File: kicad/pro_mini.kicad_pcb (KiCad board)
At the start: 2 copper layers, 17.8 x 33 mm, 15 parts, among them IC1 ATMEGA328P-A, P1 FTDI, P2 DIGITAL, P3 CONN_01X12, U1 MCP1700T-3302E

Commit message: Back silkscreen
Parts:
- added REF**: TheApiLogo, theapi_graphics:TheApiLogo, B.Cu at (110.9, 107.3)
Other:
- board text added: "3V3 8MHz internal oscillator"
- board text added: "https://github.com/theapi/pro_mini"
- board text added: "v1.0"
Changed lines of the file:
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@@
 (kicad_pcb (version 4) (host pcbnew 4.0.1-stable)
   (general
-    (links 0)
+    (links 54)
     (no_connects 0)
-    (area 99.799724 94.0002 123.323134 136.9898)
+    (area 101.524999 98.984999 119.455001 132.155001)
     (thickness 1.6)
-    (drawings 34)
+    (drawings 37)
     (tracks 280)
     (zones 0)
-    (modules 15)
+    (modules 16)
     (nets 32)
   )
   (page A4)
   (layers
-    (0 F.Cu signal)
-    (31 B.Cu signal)
+    (0 F.Cu signal hide)
+    (31 B.Cu signal hide)
     (32 B.Adhes user)
     (33 F.Adhes user)
@@
     (pad_to_mask_clearance 0.2)
     (aux_axis_origin 0 0)
-    (visible_elements 7FFFFFFF)
+    (visible_elements 7FFFFDFF)
     (pcbplotparams
       (layerselection 0x010f0_80000001)
@@
     (fp_circle (center 0.12 2.2) (end 0.15 2.21) (layer F.Mask) (width 0.15))
   )
+  (module theapi_graphics:TheApiLogo (layer B.Cu)
+    (at 110.871 107.315 180)
+    (fp_text reference REF** (at -1.45 -16.875 180) (layer B.SilkS) hide
+      (effects (font (size 1 1) (thickness 0.15)) (justify mirror))
+    )
+    (fp_text value TheApiLogo (at 0 0.5 180) (layer B.Fab)
+      (effects (font (size 1 1) (thickness 0.15)) (justify mirror))
+    )
+    (fp_line (start 2.575 -21.95) (end 3.3 -20.725) (layer B.SilkS) (width 0.15))
+    (fp_line (start 3.3 -20.725) (end 3.55 -19.725) (layer B.SilkS) (width 0.15))
+    (fp_line (start 3.55 -19.725) (end 3.925 -21.25) (layer B.SilkS) (width 0.15))
+    (fp_line (start 3.925 -21.25) (end 3.375 -22.325) (layer B.SilkS) (width 0.15))
+    (fp_line (start 3.375 -22.325) (end 2.5 -23.475) (layer B.SilkS) (width 0.15))
+    (fp_line (start 2.5 -23.475) (end 2.85 -23.3) (layer B.SilkS) (width 0.15))
+    (fp_line (start 0.35 -9.95) (end 1.25 -12.275) (layer B.SilkS) (width 0.15))
+    (fp_line (start 1.25 -12.275) (end 2.05 -13.5) (layer B.SilkS) (width 0.15))
+    (fp_line (start 2.05 -13.5) (end 2.575 -15.025) (layer B.SilkS) (width 0.15))
+    (fp_line (start 2.575 -15.025) (end 2.85 -16.725) (layer B.SilkS) (width 0.15))
+    (fp_line (start 2.85 -16.725) (end 2.95 -18.575) (layer B.SilkS) (width 0.15))
+    (fp_line (start 2.95 -18.575) (end 2.675 -20.625) (layer B.SilkS) (width 0.15))
+    (fp_line (start 2.675 -20.625) (end 2.5 -23.025) (layer B.SilkS) (width 0.15))
+    (fp_line (start 2.5 -23.025) (end 2.05 -24.525) (layer B.SilkS) (width 0.15))
+    (fp_line (start 2.05 -24.525) (end 2.05 -24.9) (layer B.SilkS) (width 0.15))
+    (fp_line (start -1.025 -7.525) (end -0.7 -8.05) (layer B.SilkS) (width 0.15))
+    (fp_line (start -0.7 -8.05) (end -0.25 -8.25) (layer B.SilkS) (width 0.15))
+    (fp_line (start -0.25 -8.25) (end 0.325 -8.475) (layer B.SilkS) (width 0.15))
+    (fp_line (start 0.325 -8.475) (end 1.1 -8.6) (layer B.SilkS) (width 0.15))
+    (fp_line (start 1.1 -8.6) (end 1.725 -8.375) (layer B.SilkS) (width 0.15))
+    (fp_line (start 1.725 -8.375) (end 2.15 -7.975) (layer B.SilkS) (width 0.15))
+    (fp_line (start 2.15 -7.975) (end 2.325 -7.3) (layer B.SilkS) (width 0.15))
+    (fp_line (start 2.325 -7.3) (end 2.225 -7.3) (layer B.SilkS) (width 0.15))
+    (fp_line (start 1.55 -5.7) (end 1.05 -5.75) (layer B.SilkS) (width 0.15))
+    (fp_line (start 1.05 -5.75) (end 0.925 -6.075) (layer B.SilkS) (width 0.15))
+    (fp_line (start 0.925 -6.075) (end 0.975 -6.525) (layer B.SilkS) (width 0.15))
+    (fp_line (start 0.975 -6.525) (end 1.6 -6.575) (layer B.SilkS) (width 0.15))
+    (fp_line (start 1.6 -6.575) (end 1.875 -6.3) (layer B.SilkS) (width 0.15))
+    (fp_line (start 1.875 -6.3) (end 1.55 -5.975) (layer B.SilkS) (width 0.15))
+    (fp_line (start -0.7 -5.7) (end -1.025 -5.925) (layer B.SilkS) (width 0.15))
+    (fp_line (start -1.025 -5.925) (end -1.025 -6.575) (layer B.SilkS) (width 0.15))
+    (fp_line (start -1.025 -6.575) (end -0.475 -6.575) (layer B.SilkS) (width 0.15))
+    (fp_line (start -0.475 -6.575) (end -0.075 -6.425) (layer B.SilkS) (width 0.15))
+    (fp_line (start -0.075 -6.425) (end -0.125 -6.025) (layer B.SilkS) (width 0.15))
+    (fp_line (start -0.125 -6.025) (end -0.4 -5.975) (layer B.SilkS) (width 0.15))
+    (fp_line (start -0.4 -5.975) (end -0.7 -5.8) (layer B.SilkS) (width 0.15))
+    (fp_line (start -0.7 -5.8) (end -0.4 -5.8) (layer B.SilkS) (width 0.15))
+    (fp_line (start 4.05 -9.5) (end 3.625 -9) (layer B.SilkS) (width 0.15))
+    (fp_line (start 3.625 -9) (end 2.725 -8.6) (layer B.SilkS) (width 0.15))
+    (fp_line (start 2.725 -8.6) (end 3.825 -8.6) (layer B.SilkS) (width 0.15))
+    (fp_line (start 3.825 -8.6) (end 5.3 -8.15) (layer B.SilkS) (width 0.15))
+    (fp_line (start 5.3 -8.15) (end 6.175 -7.6) (layer B.SilkS) (width 0.15))
+    (fp_line (start 6.175 -7.6) (end 6.475 -6.8) (layer B.SilkS) (width 0.15))
+    (fp_line (start 6.475 -6.8) (end 6.4 -6.15) (layer B.SilkS) (width 0.15))
+    (fp_line (start 6.4 -6.15) (end 6.125 -5.7) (layer B.SilkS) (width 0.15))
+    (fp_line (start 6.125 -5.7) (end 5.45 -5.25) (layer B.SilkS) (width 0.15))
+    (fp_line (start 5.45 -5.25) (end 4.775 -5.2) (layer B.SilkS) (width 0.15))
+    (fp_line (start 4.775 -5.2) (end 3.9 -5.125) (layer B.SilkS) (width 0.15))
+    (fp_line (start 3.9 -5.125) (end 3.225 -5.125) (layer B.SilkS) (width 0.15))
+    (fp_line (start 3.225 -5.125) (end 2.825 -5.125) (layer B.SilkS) (width 0.15))
+    (fp_line (start 2.825 -5.125) (end 2.825 -5.075) (layer B.SilkS) (width 0.15))
+    (fp_line (start -2.15 -5.575) (end -3.15 -5.75) (layer B.SilkS) (width 0.15))
+    (fp_line (start -3.15 -5.75) (end -3.875 -5.925) (layer B.SilkS) (width 0.15))
+    (fp_line (start -3.875 -5.925) (end -4.65 -6.35) (layer B.SilkS) (width 0.15))
+    (fp_line (start -4.65 -6.35) (end -5.325 -6.925) (layer B.SilkS) (width 0.15))
+    (fp_line (start -5.325 -6.925) (end -5.45 -8.1) (layer B.SilkS) (width 0.15))
+    (fp_line (start -5.45 -8.1) (end -5 -9) (layer B.SilkS) (width 0.15))
+    (fp_line (start -5 -9) (end -4.15 -9.375) (layer B.SilkS) (width 0.15))
+    (fp_line (start -4.15 -9.375) (end -3.1 -9.275) (layer B.SilkS) (width 0.15))
+    (fp_line (start -3.1 -9.275) (end -2.475 -8.875) (layer B.SilkS) (width 0.15))
+    (fp_line (start -2.475 -8.875) (end -2.025 -8.6) (layer B.SilkS) (width 0.15))
+    (fp_line (start -2.025 -8.6) (end -2.525 -9.325) (layer B.SilkS) (width 0.15))
+    (fp_line (start -2.525 -9.325) (end -2.925 -10.55) (layer B.SilkS) (width 0.15))
+    (fp_line (start -2.925 -10.55) (end -2.7 -11.45) (layer B.SilkS) (width 0.15))
+    (fp_line (start -2.7 -11.45) (end -2.2 -12.225) (layer B.SilkS) (width 0.15))
+    (fp_line (start -2.2 -12.225) (end -1.35 -12.35) (layer B.SilkS) (width 0.15))
+    (fp_line (start -1.35 -12.35) (end -0.175 -12.125) (layer B.SilkS) (width 0.15))
+    (fp_line (start -0.175 -12.125) (end 0.25 -11.5) (layer B.SilkS) (width 0.15))
+    (fp_line (start 0.25 -11.5) (end 0.425 -10.775) (layer B.SilkS) (width 0.15))
+    (fp_line (start 0.425 -10.775) (end 0.375 -9.95) (layer B.SilkS) (width 0.15))
+    (fp_line (start 0.375 -9.95) (end 0.825 -10.675) (layer B.SilkS) (width 0.15))
+    (fp_line (start 0.825 -10.675) (end 1.275 -11.225) (layer B.SilkS) (width 0.15))
+    (fp_line (start 1.275 -11.225) (end 2.375 -11.85) (layer B.SilkS) (width 0.15))
+    (fp_line (start 2.375 -11.85) (end 3.5 -11.775) (layer B.SilkS) (width 0.15))
+    (fp_line (start 3.5 -11.775) (end 4.4 -11) (layer B.SilkS) (width 0.15))
+    (fp_line (start 4.4 -11) (end 4.45 -10.15) (layer B.SilkS) (width 0.15))
+    (fp_line (start 4.45 -10.15) (end 4 -9.425) (layer B.SilkS) (width 0.15))
+    (fp_line (start 0.425 -3.95) (end -0.025 -3.175) (layer B.SilkS) (width 0.15))
+    (fp_line (start -0.025 -3.175) (end -0.7 -2.625) (layer B.SilkS) (width 0.15))
+    (fp_line (start -0.7 -2.625) (end -1.475 -2.125) (layer B.SilkS) (width 0.15))
+    (fp_line (start -1.475 -2.125) (end -2.875 -2) (layer B.SilkS) (width 0.15))
+    (fp_line (start -2.875 -2) (end -3.775 -2.45) (layer B.SilkS) (width 0.15))
+    (fp_line (start -3.775 -2.45) (end -4.325 -3.3) (layer B.SilkS) (width 0.15))
+    (fp_line (start -4.325 -3.3) (end -4.275 -4.3) (layer B.SilkS) (width 0.15))
+    (fp_line (start -4.275 -4.3) (end -3.65 -5.125) (layer B.SilkS) (width 0.15))
+    (fp_line (start -3.65 -5.125) (end -2.875 -5.3) (layer B.SilkS) (width 0.15))
+    (fp_line (start -2.875 -5.3) (end -2.025 -5.475) (layer B.SilkS) (width 0.15))
+    (fp_line (start -2.025 -5.475) (end -2.075 -5.7) (layer B.SilkS) (width 0.15))
+    (fp_line (start 0.475 -3.95) (end 0.65 -2.9) (layer B.SilkS) (width 0.15))
+    (fp_line (start 0.65 -2.9) (end 1.15 -2) (layer B.SilkS) (width 0.15))
+    (fp_line (start 1.15 -2) (end 2.375 -1.325) (layer B.SilkS) (width 0.15))
+    (fp_line (start 2.375 -1.325) (end 3.775 -1.45) (layer B.SilkS) (width 0.15))
+    (fp_line (start 3.775 -1.45) (end 4.625 -2.225) (layer B.SilkS) (width 0.15))
+    (fp_line (start 4.625 -2.225) (end 4.85 -3.35) (layer B.SilkS) (width 0.15))
+    (fp_line (start 4.85 -3.35) (end 4.225 -4.3) (layer B.SilkS) (width 0.15))
+    (fp_line (start 4.225 -4.3) (end 3.4 -4.9) (layer B.SilkS) (width 0.15))
+    (fp_line (start 3.4 -4.9) (end 2.775 -5.125) (layer B.SilkS) (width 0.15))
+    (fp_circle (center 0.4 -6.87) (end 2.94 -5.6) (layer B.SilkS) (width 0.15))
+  )
+  (gr_text v1.0 (at 110.744 130.937 360) (layer B.SilkS)
+    (effects (font (size 1.016 1.016) (thickness 0.2032)) (justify mirror))
+  )
+  (gr_text "3V3 8MHz\ninternal\noscillator" (at 110.49 104.775) (layer B.SilkS)
+    (effects (font (size 1.016 1.016) (thickness 0.2032)) (justify mirror))
+  )
+  (gr_text https://github.com/theapi/pro_mini (at 115.824 116.713 90) (layer B.SilkS)
+    (effects (font (size 1.016 1.016) (thickness 0.2032)) (justify mirror))
+  )
   (gr_text VCC (at 116.332 110.49 90) (layer F.SilkS)

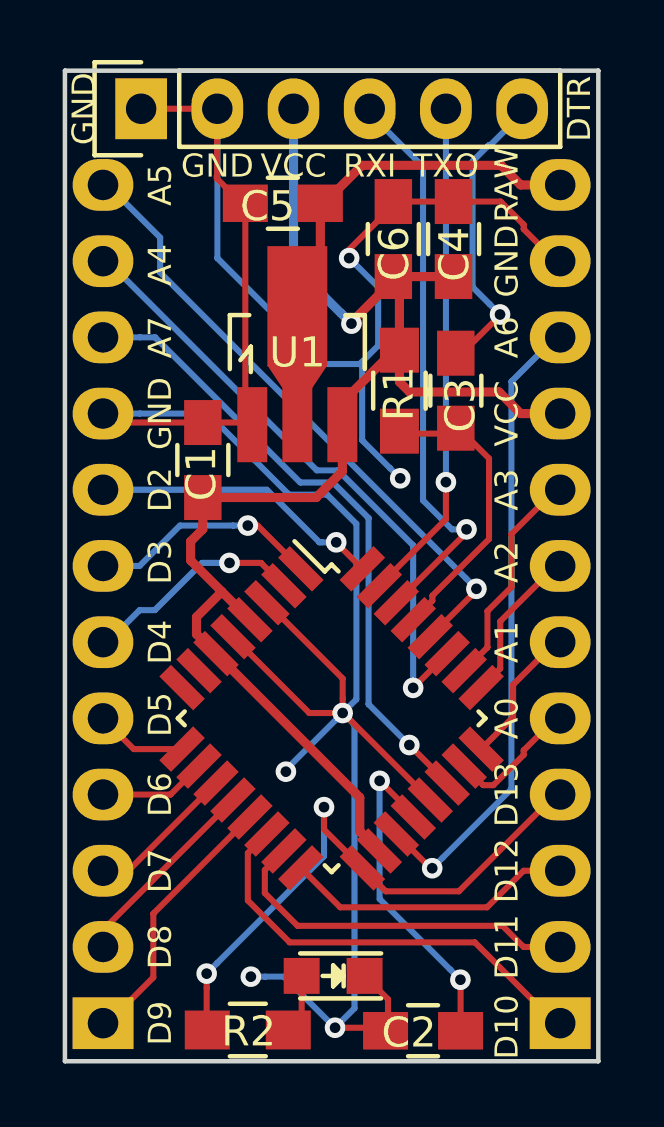
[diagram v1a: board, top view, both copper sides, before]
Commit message: Optional external oscillator & reset restored to side header
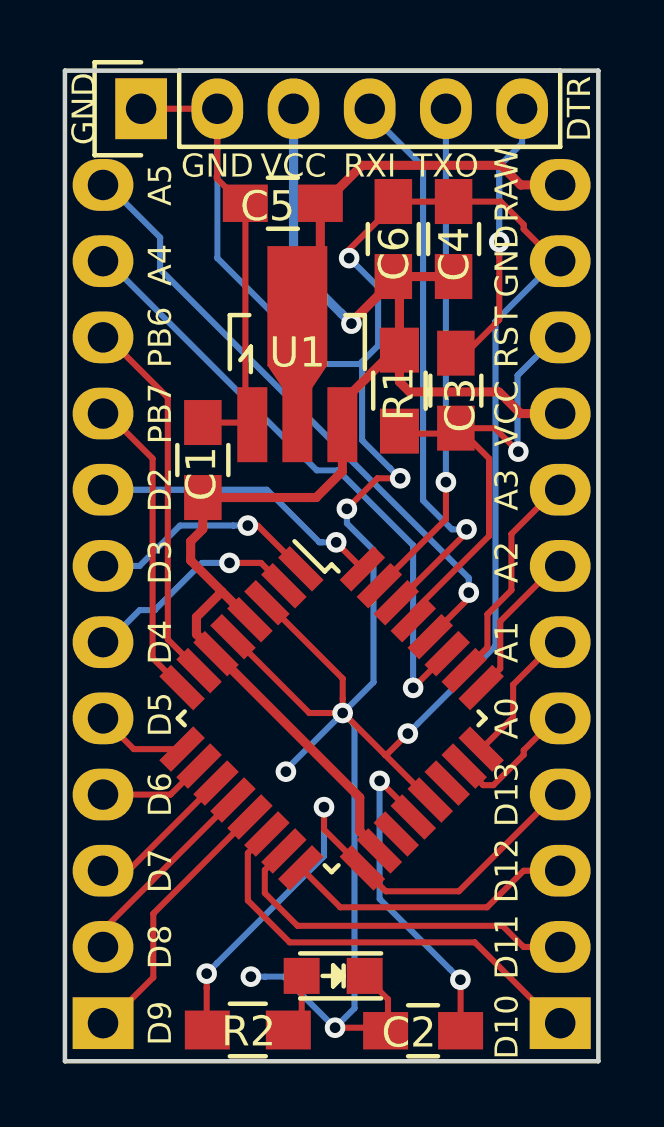
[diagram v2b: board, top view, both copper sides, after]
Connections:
- C3 pad 1: /RESET -> RESET
- IC1 pad 19: A6 -> Net-(IC1-Pad19)
- IC1 pad 22: A7 -> Net-(IC1-Pad22)
- IC1 pad 29: /RESET -> RESET
- IC1 pad 7: Net-(IC1-Pad7) -> PB6
- IC1 pad 8: Net-(IC1-Pad8) -> PB7
- P2 pad 10: A7 -> PB6
- P2 pad 9: GND -> PB7
- P3 pad 10: A6 -> RESET
- R1 pad 2: /RESET -> RESET
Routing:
- net A7: track 21.3 -> 0.00 mm, vias 1 -> 0
- net A6: track 21.2 -> 0.00 mm, vias 1 -> 0
- net RESET: track 0.00 -> 16.6 mm, vias 0 -> 1
- net PB6: track 0.00 -> 12.5 mm
- net PB7: track 0.00 -> 10.7 mm
- net /RESET: track 9.67 -> 0.00 mm
- net GND: track 98.9 -> 107.8 mm, vias 6 -> 8
- net DTR: track 9.79 -> 9.00 mm
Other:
- board text added: "3V3 8MHz"
- board text added: "PB6"
- board text added: "PB7"
- board text added: "RST"
- board text removed: "3V3 8MHz internal oscillator"
- board text removed: "A6"
- board text removed: "A7"
